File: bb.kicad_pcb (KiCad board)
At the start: 2 copper layers, 162 x 153.9 mm, 49 parts, among them J2 AudioJack2, J4 USB_C_Receptacle_PowerOnly_6P, Q1 BC547/S9014, Q2 BC547/S9014, SW1 SW_DPST_x2, U1 ESP-12F, U2 LM1117MP-3.3

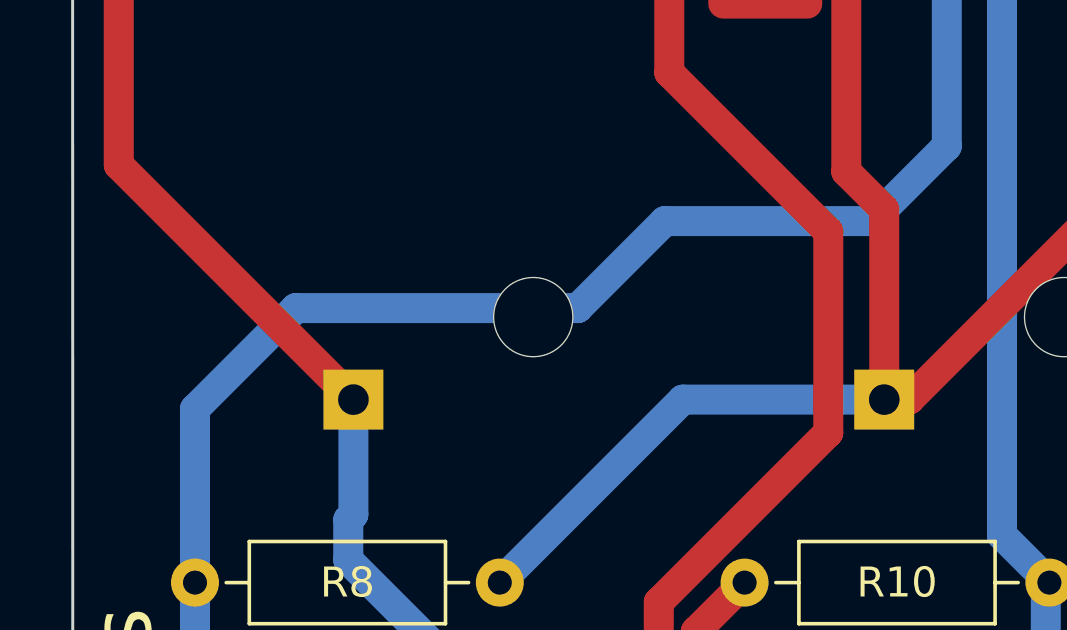
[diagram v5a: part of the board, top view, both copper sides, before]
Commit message: hotfix: A0 cut by hole
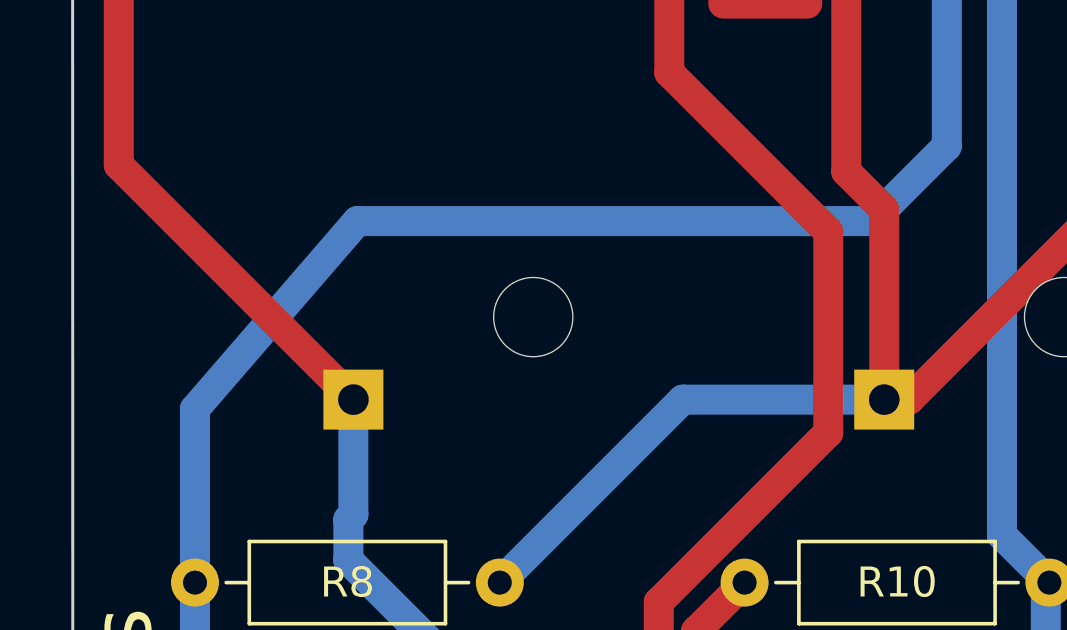
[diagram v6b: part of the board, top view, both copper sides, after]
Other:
- board text removed: "the gnd of esp is missing in version 0.2"
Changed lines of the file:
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@@
 		(fp_arc
 			(start 0.215816 -1.115611)
-			(mid 0.446099 -1.502142)
+			(mid 0.4461 -1.502142)
 			(end 0.74 -1.842816)
 			(stroke
@@
 		(fp_arc
 			(start 4.896401 1.10599)
-			(mid 3.936978 2.2)
+			(mid 3.936978 2.199999)
 			(end 2.54 2.607183)
 			(stroke
@@
 		(layer "Edge.Cuts")
 	)
-	(gr_circle
-		(center 117.066905 112.9)
-		(end 121.73381 112.9)
-		(stroke
-			(width 1)
-			(type default)
-		)
-		(fill none)
-		(layer "User.3")
-	)
 	(gr_text "l  e  d   d  i  f  f  u  s  e  r "
 		(at 134.6 58.2 0)
@@
 		)
 	)
-	(gr_text "the gnd of esp is missing in version 0.2"
-		(at 127.2 113.8 0)
-		(layer "User.3")
-		(effects
-			(font
-				(size 1 1)
-				(thickness 0.15)
-			)
-			(justify left bottom)
-		)
-	)
 	(segment
 		(start 61.845712 69.75)
@@
 	)
 	(segment
-		(start 108.95 152.7)
-		(end 115.85 152.7)
-		(width 1)
-		(layer "B.Cu")
-		(net 39)
-	)
-	(segment
 		(start 133.402944 87.2)
 		(end 118.6 102.002944)
@@
 	)
 	(segment
-		(start 96.65 155.6)
-		(end 106.05 155.6)
+		(start 93.290225 164.75)
+		(end 93.290225 158.959775)
 		(width 1)
 		(layer "B.Cu")
@@
 	)
 	(segment
-		(start 93.270225 169.07)
-		(end 93.290225 169.05)
+		(start 118.6 108)
+		(end 118.6 105.6)
 		(width 1)
 		(layer "B.Cu")
@@
 	)
 	(segment
-		(start 118.6 108)
-		(end 118.6 105.6)
+		(start 93.270225 169.07)
+		(end 93.290225 169.05)
 		(width 1)
 		(layer "B.Cu")
@@
 	)
 	(segment
-		(start 106.05 155.6)
-		(end 108.95 152.7)
-		(width 1)
-		(layer "B.Cu")
-		(net 39)
-	)
-	(segment
 		(start 133.7 87.2)
 		(end 133.402944 87.2)
@@
 	)
 	(segment
-		(start 118.35 108.25)
-		(end 118.6 108)
+		(start 118.35 150.2)
+		(end 118.35 108.25)
+		(width 1)
+		(layer "B.Cu")
+		(net 39)
+	)
+	(segment
+		(start 115.85 152.7)
+		(end 118.35 150.2)
+		(width 1)
+		(layer "B.Cu")
+		(net 39)
+	)
+	(segment
+		(start 93.290225 158.959775)
+		(end 98.7 152.7)
 		(width 1)
 		(layer "B.Cu")
@@
 	)
 	(segment
+		(start 98.7 152.7)
+		(end 115.85 152.7)
+		(width 1)
+		(layer "B.Cu")
+		(net 39)
+	)
+	(segment
 		(start 115.1 97.8)
 		(end 115.1 100.4)
@@
 	)
 	(segment
-		(start 93.290225 158.959775)
-		(end 96.65 155.6)
-		(width 1)
-		(layer "B.Cu")
-		(net 39)
-	)
-	(segment
 		(start 137.45 87.3)
 		(end 136.505534 86.355534)
@@
 	)
 	(segment
-		(start 118.35 150.2)
-		(end 118.35 108.25)
-		(width 1)
-		(layer "B.Cu")
-		(net 39)
-	)
-	(segment
-		(start 115.85 152.7)
-		(end 118.35 150.2)
-		(width 1)
-		(layer "B.Cu")
-		(net 39)
-	)
-	(segment
-		(start 93.290225 164.75)
-		(end 93.290225 158.959775)
+		(start 118.35 108.25)
+		(end 118.6 108)
 		(width 1)
 		(layer "B.Cu")
